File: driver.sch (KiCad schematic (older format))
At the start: 26 parts, among them Q1 Q_NMOS_GDSD, Q10 Q_NMOS_GDSD, Q11 Q_NMOS_GDSD, Q12 Q_NMOS_GDSD, Q13 Q_NMOS_GDSD, Q14 Q_NMOS_GDSD, Q15 Q_NMOS_GDSD, Q16 Q_NMOS_GDSD, Q2 Q_NMOS_GDSD, Q3 Q_NMOS_GDSD, Q4 Q_NMOS_GDSD, Q5 Q_NMOS_GDSD, Q6 Q_NMOS_GDSD, Q7 Q_NMOS_GDSD, Q8 Q_NMOS_GDSD, Q9 Q_NMOS_GDSD, U1 PCA9685PW

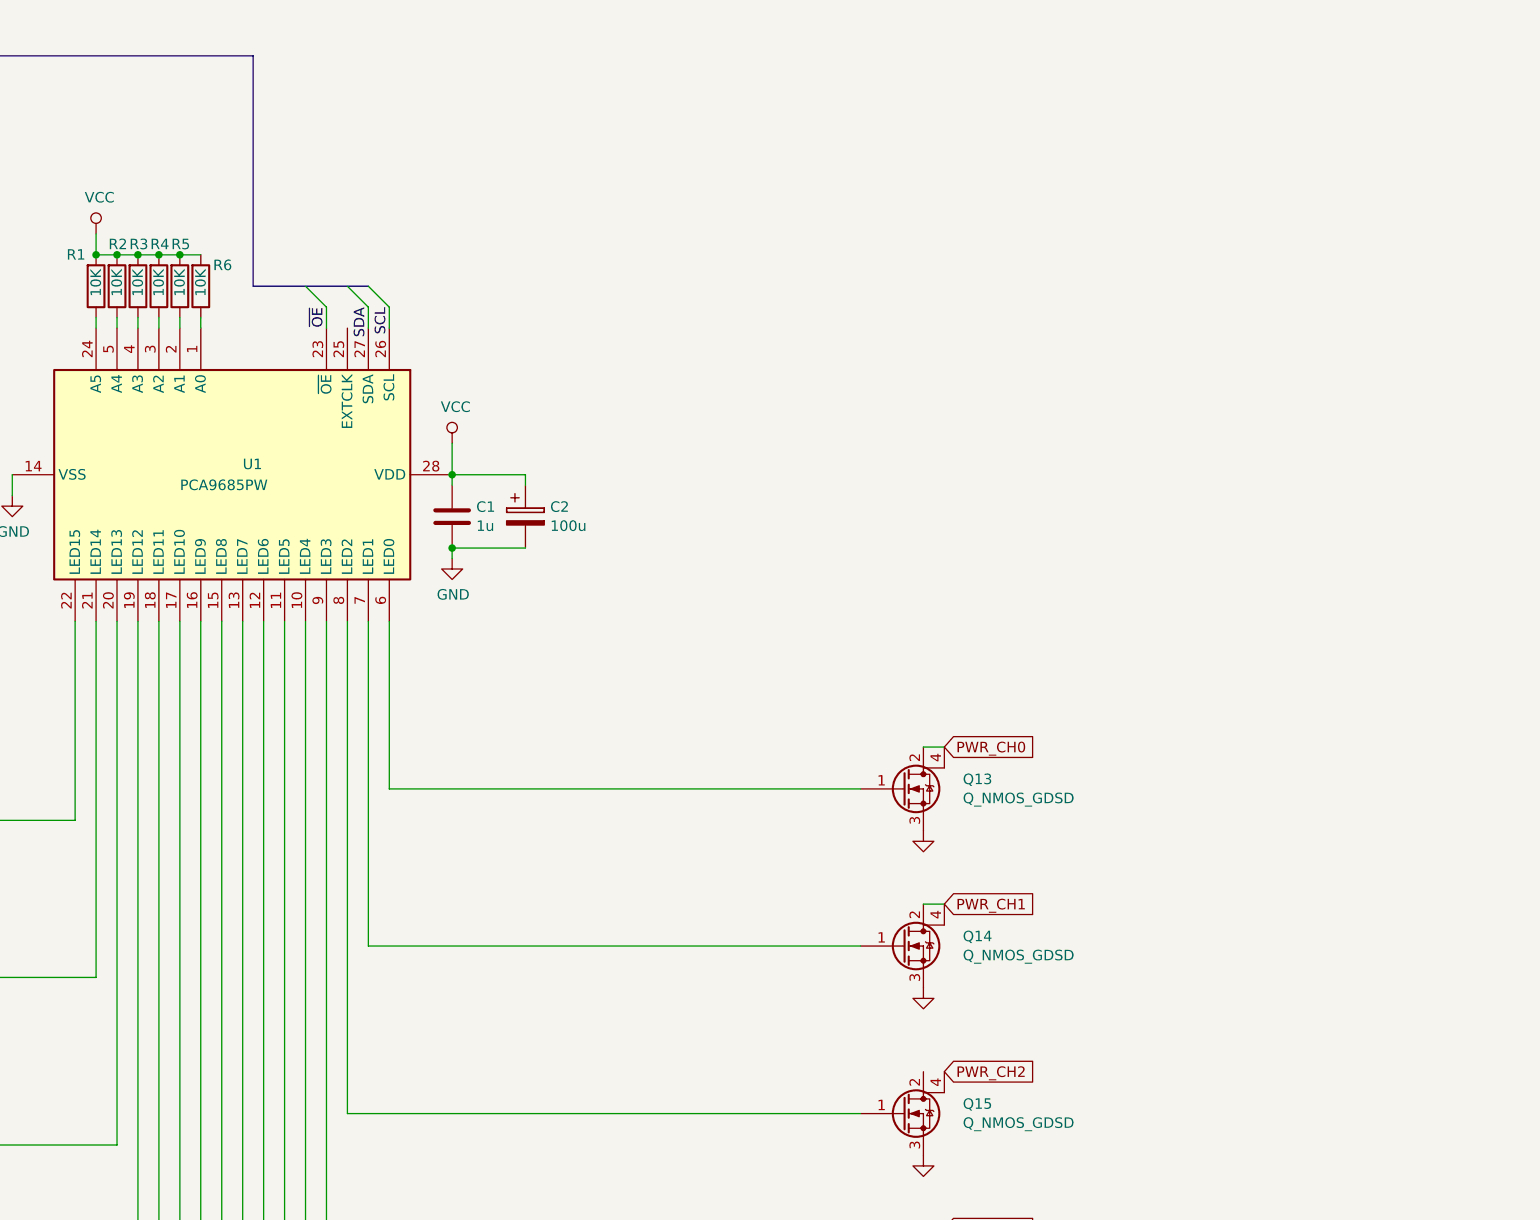
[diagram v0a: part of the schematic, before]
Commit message: 28V heater power input, reverse polarity protection, early BOM
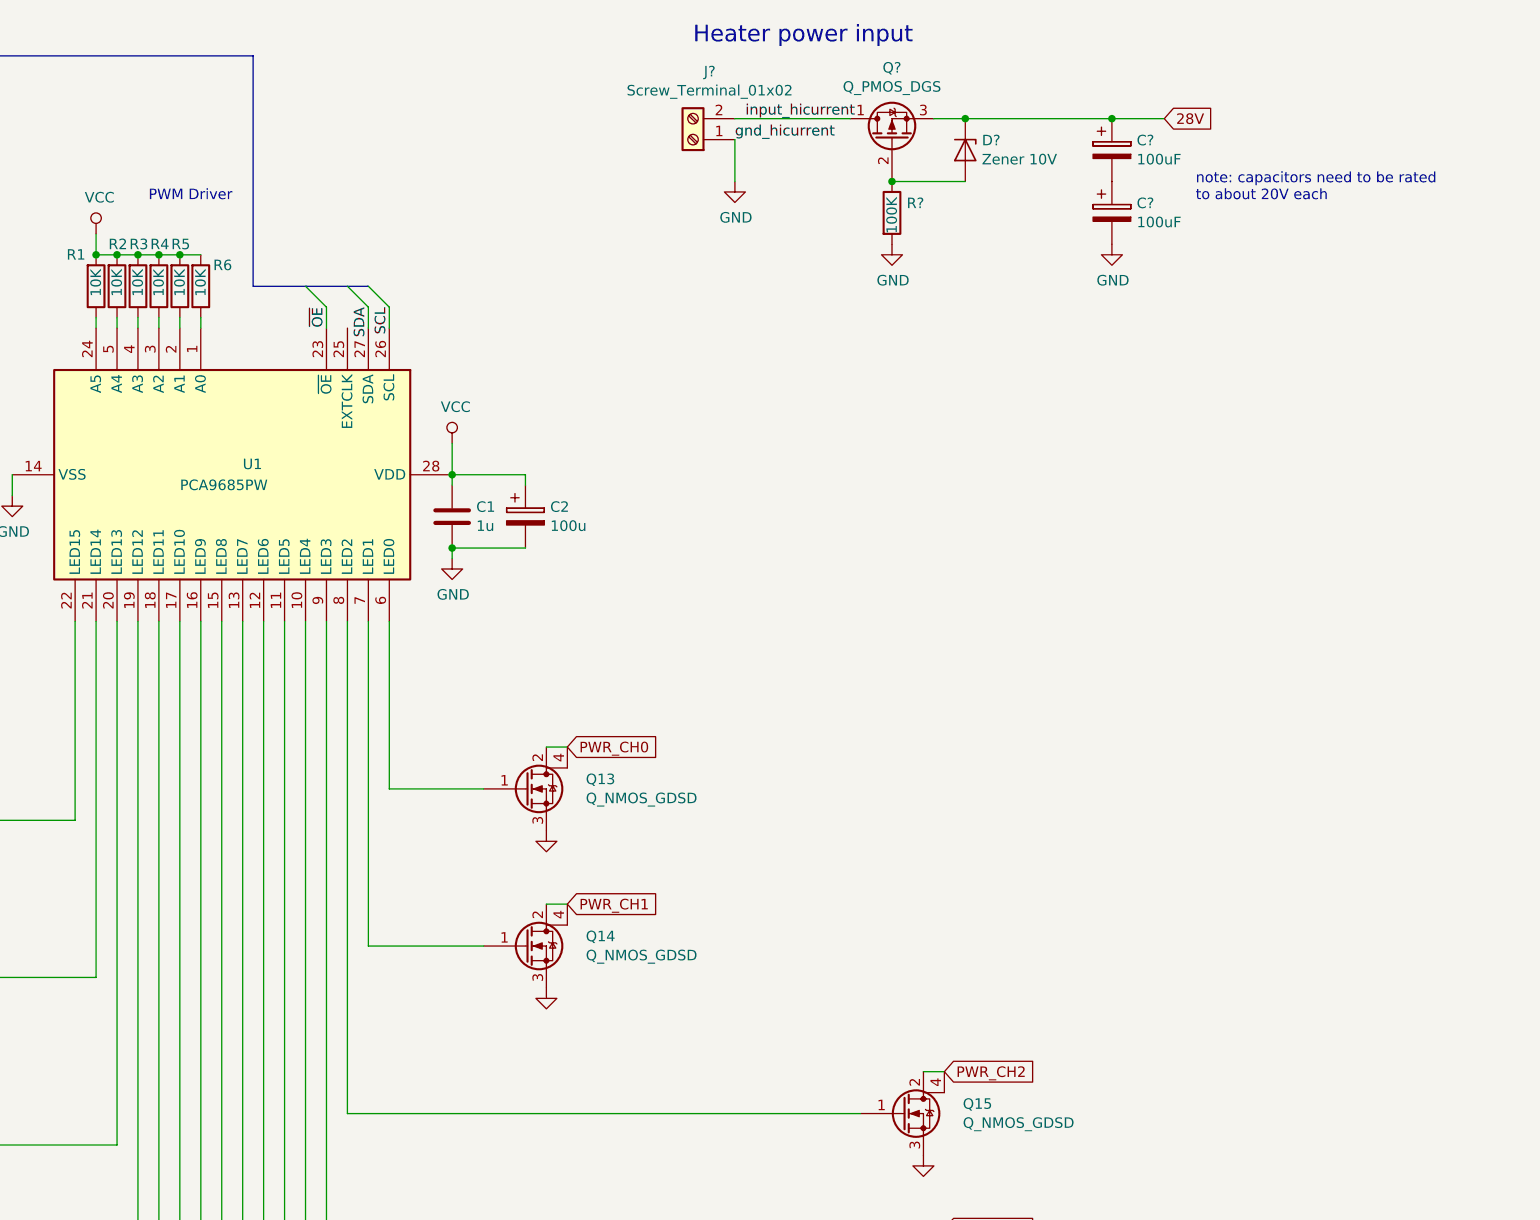
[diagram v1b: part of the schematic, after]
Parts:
- added C? (x2): 100uF, symbol Device:CP
- added D?: Zener 10V, symbol Device:D_Zener
- added J?: Screw_Terminal_01x02, symbol Connector:Screw_Terminal_01x02
- added Q?: Q_PMOS_DGS, symbol Device:Q_PMOS_DGS
- added R?: 100K, symbol Device:R
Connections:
- net GND: now also C?.2, J?.1 (Pin_1), R?.2
- net PWR_CH2: now also Q15.2 (D)
- new net: D?.2 (A), Q?.2 (G), R?.1
- new net: C?.1, C?.2
- new net 28V: C?.1, D?.1 (K), Q?.3 (S)
- new net input_hicurrent: J?.2 (Pin_2), Q?.1 (D)
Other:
- note added: "Heater power input"
- note added: "PWM Driver"
- note added: "note: capacitors need to be rated\nto about 20V each"
- moved on the sheet: Q13, Q14
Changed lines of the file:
@@
 L Device:Q_NMOS_GDSD Q13
 U 1 1 5C4266CB
-P 8950 4550
-F 0 "Q13" H 9238 4596 50  0000 L CNN
-F 1 "Q_NMOS_GDSD" H 9238 4505 50  0000 L CNN
-F 2 "Package_TO_SOT_SMD:SOT-223" H 9150 4650 50  0001 C CNN
-F 3 "~" H 8950 4550 50  0001 C CNN
-	1    8950 4550
+P 7150 4550
+F 0 "Q13" H 7438 4596 50  0000 L CNN
+F 1 "Q_NMOS_GDSD" H 7438 4505 50  0000 L CNN
+F 2 "Package_TO_SOT_SMD:SOT-223" H 7350 4650 50  0001 C CNN
+F 3 "~" H 7150 4550 50  0001 C CNN
+	1    7150 4550
 	1    0    0    -1
 $EndComp
@@
 L Device:Q_NMOS_GDSD Q14
 U 1 1 5C4266D2
-P 8950 5300
-F 0 "Q14" H 9238 5346 50  0000 L CNN
-F 1 "Q_NMOS_GDSD" H 9238 5255 50  0000 L CNN
-F 2 "Package_TO_SOT_SMD:SOT-223" H 9150 5400 50  0001 C CNN
-F 3 "~" H 8950 5300 50  0001 C CNN
-	1    8950 5300
+P 7150 5300
+F 0 "Q14" H 7438 5346 50  0000 L CNN
+F 1 "Q_NMOS_GDSD" H 7438 5255 50  0000 L CNN
+F 2 "Package_TO_SOT_SMD:SOT-223" H 7350 5400 50  0001 C CNN
+F 3 "~" H 7150 5300 50  0001 C CNN
+	1    7150 5300
 	1    0    0    -1
 $EndComp
@@
 L power:GND #PWR013
 U 1 1 5C4266D9
-P 9050 4750
-F 0 "#PWR013" H 9050 4500 50  0001 C CNN
-F 1 "GND" H 9055 4577 50  0001 C CNN
-F 2 "" H 9050 4750 50  0001 C CNN
-F 3 "" H 9050 4750 50  0001 C CNN
-	1    9050 4750
+P 7250 4750
+F 0 "#PWR013" H 7250 4500 50  0001 C CNN
+F 1 "GND" H 7255 4577 50  0001 C CNN
+F 2 "" H 7250 4750 50  0001 C CNN
+F 3 "" H 7250 4750 50  0001 C CNN
+	1    7250 4750
 	-1   0    0    -1
 $EndComp
@@
 L power:GND #PWR014
 U 1 1 5C4266DF
-P 9050 5500
-F 0 "#PWR014" H 9050 5250 50  0001 C CNN
-F 1 "GND" H 9055 5327 50  0001 C CNN
-F 2 "" H 9050 5500 50  0001 C CNN
-F 3 "" H 9050 5500 50  0001 C CNN
-	1    9050 5500
+P 7250 5500
+F 0 "#PWR014" H 7250 5250 50  0001 C CNN
+F 1 "GND" H 7255 5327 50  0001 C CNN
+F 2 "" H 7250 5500 50  0001 C CNN
+F 3 "" H 7250 5500 50  0001 C CNN
+	1    7250 5500
 	-1   0    0    -1
 $EndComp
-Text GLabel 9150 4350 2    50   Input ~ 0
+Text GLabel 7350 4350 2    50   Input ~ 0
 PWR_CH0
 Wire Wire Line
-	9150 4350 9050 4350
-Wire Wire Line
-	8750 4550 6500 4550
+	6950 4550 6500 4550
 Wire Wire Line
 	6500 4550 6500 3750
@@
 	6400 3750 6400 5300
 Wire Wire Line
-	6400 5300 8750 5300
-Text GLabel 9150 5100 2    50   Input ~ 0
+	6400 5300 6950 5300
+Text GLabel 7350 5100 2    50   Input ~ 0
 PWR_CH1
 Wire Wire Line
-	9150 5100 9050 5100
+	7350 5100 7250 5100
 Text GLabel 9150 5900 2    50   Input ~ 0
 PWR_CH2
@@
 Wire Wire Line
 	3100 4700 5000 4700
+Text Notes 7950 1000 0    79   ~ 0
+Heater power input
+$Comp
+L Connector:Screw_Terminal_01x02 J?
+U 1 1 5C429E96
+P 7950 1450
+F 0 "J?" H 7870 1125 50  0000 C CNN
+F 1 "Screw_Terminal_01x02" H 7870 1216 50  0000 C CNN
+F 2 "" H 7950 1450 50  0001 C CNN
+F 3 "~" H 7950 1450 50  0001 C CNN
+	1    7950 1450
+	-1   0    0    1
+$EndComp
+$Comp
+L Device:Q_PMOS_DGS Q?
+U 1 1 5C429FD6
+P 8900 1450
+F 0 "Q?" V 9243 1450 50  0000 C CNN
+F 1 "Q_PMOS_DGS" V 9152 1450 50  0000 C CNN
+F 2 "" H 9100 1550 50  0001 C CNN
+F 3 "~" H 8900 1450 50  0001 C CNN
+	1    8900 1450
+	0    -1   -1   0
+$EndComp
+Wire Wire Line
+	8150 1350 8700 1350
+$Comp
+L Device:D_Zener D?
+U 1 1 5C42C2C0
+P 9250 1500
+F 0 "D?" V 9204 1579 50  0000 L CNN
+F 1 "Zener 10V" V 9295 1579 50  0000 L CNN
+F 2 "" H 9250 1500 50  0001 C CNN
+F 3 "~" H 9250 1500 50  0001 C CNN
+	1    9250 1500
+	0    1    1    0
+$EndComp
+Wire Wire Line
+	9100 1350 9250 1350
+$Comp
+L power:GND #PWR?
+U 1 1 5C43070B
+P 8150 1650
+F 0 "#PWR?" H 8150 1400 50  0001 C CNN
+F 1 "GND" H 8155 1477 50  0000 C CNN
+F 2 "" H 8150 1650 50  0001 C CNN
+F 3 "" H 8150 1650 50  0001 C CNN
+	1    8150 1650
+	1    0    0    -1
+$EndComp
+Wire Wire Line
+	8150 1450 8150 1650
+$Comp
+L Device:R R?
+U 1 1 5C434B34
+P 8900 1800
+F 0 "R?" H 8970 1846 50  0000 L CNN
+F 1 "100K" V 8900 1700 50  0000 L CNN
+F 2 "" V 8830 1800 50  0001 C CNN
+F 3 "~" H 8900 1800 50  0001 C CNN
+	1    8900 1800
+	1    0    0    -1
+$EndComp
+Wire Wire Line
+	9250 1650 8900 1650
+Connection ~ 8900 1650
+$Comp
+L power:GND #PWR?
+U 1 1 5C437281
+P 8900 1950
+F 0 "#PWR?" H 8900 1700 50  0001 C CNN
+F 1 "GND" H 8905 1777 50  0000 C CNN
+F 2 "" H 8900 1950 50  0001 C CNN
+F 3 "" H 8900 1950 50  0001 C CNN
+	1    8900 1950
+	1    0    0    -1
+$EndComp
+Text GLabel 10200 1350 2    50   Input ~ 0
+28V
+Connection ~ 9250 1350
+Text Label 8200 1350 0    50   ~ 0
+input_hicurrent
+Text Label 8150 1450 0    50   ~ 0
+gnd_hicurrent
+Text Notes 5350 1750 0    50   ~ 0
+PWM Driver
+Wire Wire Line
+	9250 1350 9950 1350
+$Comp
+L Device:CP C?
+U 1 1 5C43F9F2
+P 9950 1500
+F 0 "C?" H 10068 1546 50  0000 L CNN
+F 1 "100uF" H 10068 1455 50  0000 L CNN
+F 2 "" H 9988 1350 50  0001 C CNN
+F 3 "~" H 9950 1500 50  0001 C CNN
+	1    9950 1500
+	1    0    0    -1
+$EndComp
+Connection ~ 9950 1350
+Wire Wire Line
+	9950 1350 10200 1350
+$Comp
+L power:GND #PWR?
+U 1 1 5C43FABC
+P 9950 1950
+F 0 "#PWR?" H 9950 1700 50  0001 C CNN
+F 1 "GND" H 9955 1777 50  0000 C CNN
+F 2 "" H 9950 1950 50  0001 C CNN
+F 3 "" H 9950 1950 50  0001 C CNN
+	1    9950 1950
+	1    0    0    -1
+$EndComp
+$Comp
+L Device:CP C?
+U 1 1 5C43FB71
+P 9950 1800
+F 0 "C?" H 10068 1846 50  0000 L CNN
+F 1 "100uF" H 10068 1755 50  0000 L CNN
+F 2 "" H 9988 1650 50  0001 C CNN
+F 3 "~" H 9950 1800 50  0001 C CNN
+	1    9950 1800
+	1    0    0    -1
+$EndComp
+Text Notes 10350 1750 0    50   ~ 0
+note: capacitors need to be rated\nto about 20V each
+Wire Wire Line
+	7250 4350 7350 4350
+Wire Wire Line
+	9050 5900 9150 5900
 Wire Bus Line
 	5850 2150 6400 2150
